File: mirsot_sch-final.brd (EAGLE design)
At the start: 79 x 79 mm, 42 parts, among them IC1 7805T, IC2 MEGA16-P, M1 WIRELESS-NRF24L01

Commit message: finalized pcb
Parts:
- removed CN2: (no value), adafruit:JST-PH-2-THM
- added J1: XT60-M, XT60-M:AMASS_XT60-M
- moved C8 19.3 mm to (66.1, 69.6), turned to 0 degrees
- moved C1 17.1 mm to (22.8, 23.5), turned to 0 degrees
- moved IC1 11.7 mm to (18.6, 9.52), turned to 180 degrees
- moved M1 9.76 mm to (70.0, 60.4), turned to 0 degrees
- moved C5 9.66 mm to (13.0, 19.8), turned to 180 degrees
- moved C4 2.55 mm to (10.0, 7.73)
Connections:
- net GND: now also J1.N; no longer CN2.2
- net VCC: now also J1.P; no longer CN2.1
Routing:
- net +5V_SUPPLY: track 80.8 -> 54.4 mm
- net VCC: track 85.7 -> 111.1 mm
- net GND: track 0.00 -> 11.5 mm
- net CE: track 40.5 -> 48.2 mm
- net SCK: track 35.1 -> 41.7 mm
- net IRQ: track 55.3 -> 51.8 mm
- net MISO: track 38.8 -> 41.2 mm
- net +3V3: track 118.9 -> 117.1 mm
- net CSN: track 56.8 -> 58.5 mm
- net BIN1: track 27.0 -> 28.5 mm
- net RX: track 90.5 -> 92.0 mm
- net MOSI: track 48.5 -> 47.6 mm
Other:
- outline, holes or cut-outs redrawn

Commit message: changed battery connecter orientation
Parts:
- removed J1: XT60-M, XT60-M:AMASS_XT60-M
- added U$1: T_PLUG_CONNECTOR_H, con-T-plug:T_PLUG_CONNECTOR_H
- IC1: value 7805T -> 7805DT; device linear:TO220H -> linear:TO252
- moved IC1 13.2 mm to (10.5, 19.9), turned to 90 degrees
- moved C8 12.5 mm to (53.9, 66.7), turned to 270 degrees
- moved C4 11.3 mm to (18.5, 15.3), turned to 90 degrees
- moved C5 5.74 mm to (18.5, 21.5), turned to 270 degrees
- moved C1 4.32 mm to (22.0, 19.2), turned to 90 degrees
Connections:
- net +5V_SUPPLY: now also IC1.2; no longer IC1.3
- net GND: now also IC1.3, U$1.P$1; no longer IC1.2, J1.N
- net VCC: now also U$1.P$2; no longer J1.P
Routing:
- net +5V: track 32.9 -> 68.6 mm, vias 6 -> 8
- net VCC: track 111.1 -> 80.6 mm, vias 0 -> 1
- net +5V_SUPPLY: track 54.4 -> 65.1 mm
- net GND: track 11.5 -> 18.1 mm, vias 0 -> 1
- net +3V3: track 117.1 -> 111.3 mm
- net AIN2: track 57.2 -> 61.3 mm
- net LED_1: track 21.8 -> 20.9 mm
- net CE: track 48.2 -> 47.4 mm
- net SCK: track 41.7 -> 41.1 mm
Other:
- outline, holes or cut-outs redrawn

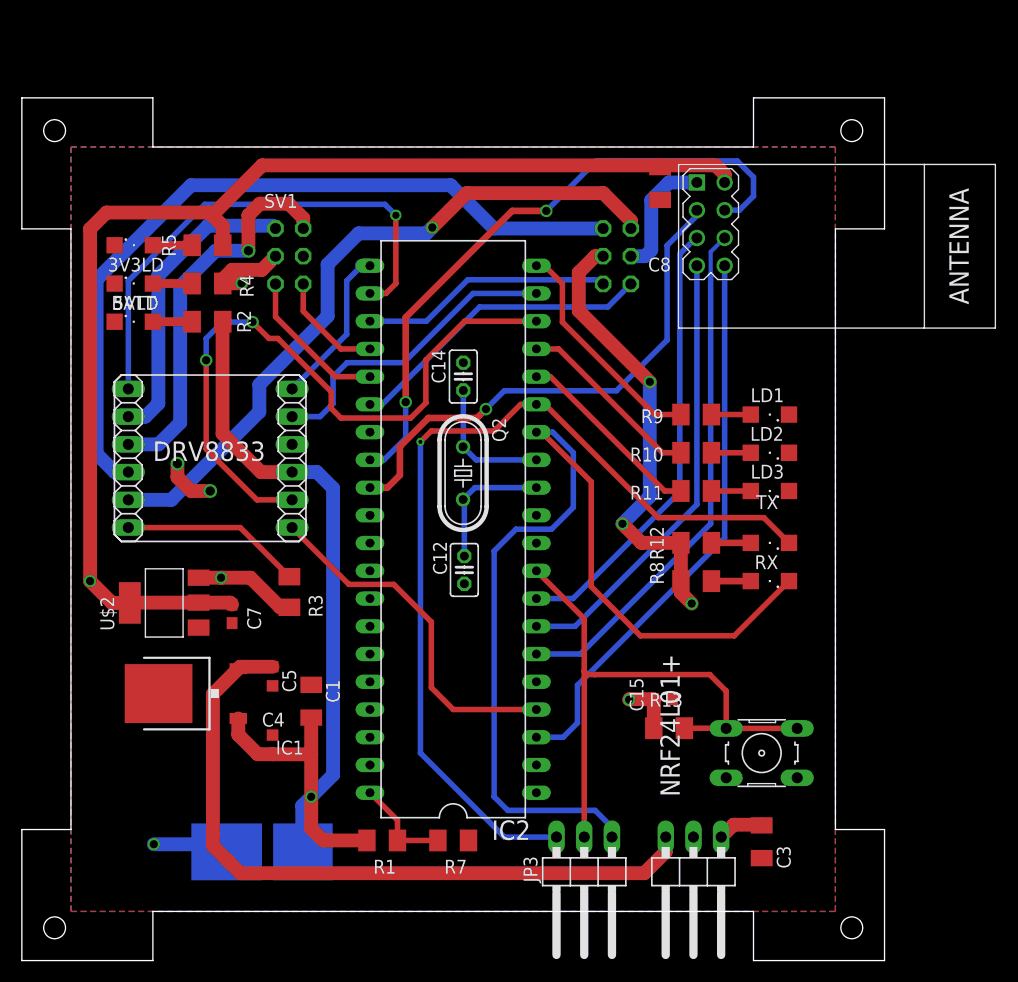
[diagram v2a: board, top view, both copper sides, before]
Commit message: changed mcu to esp32
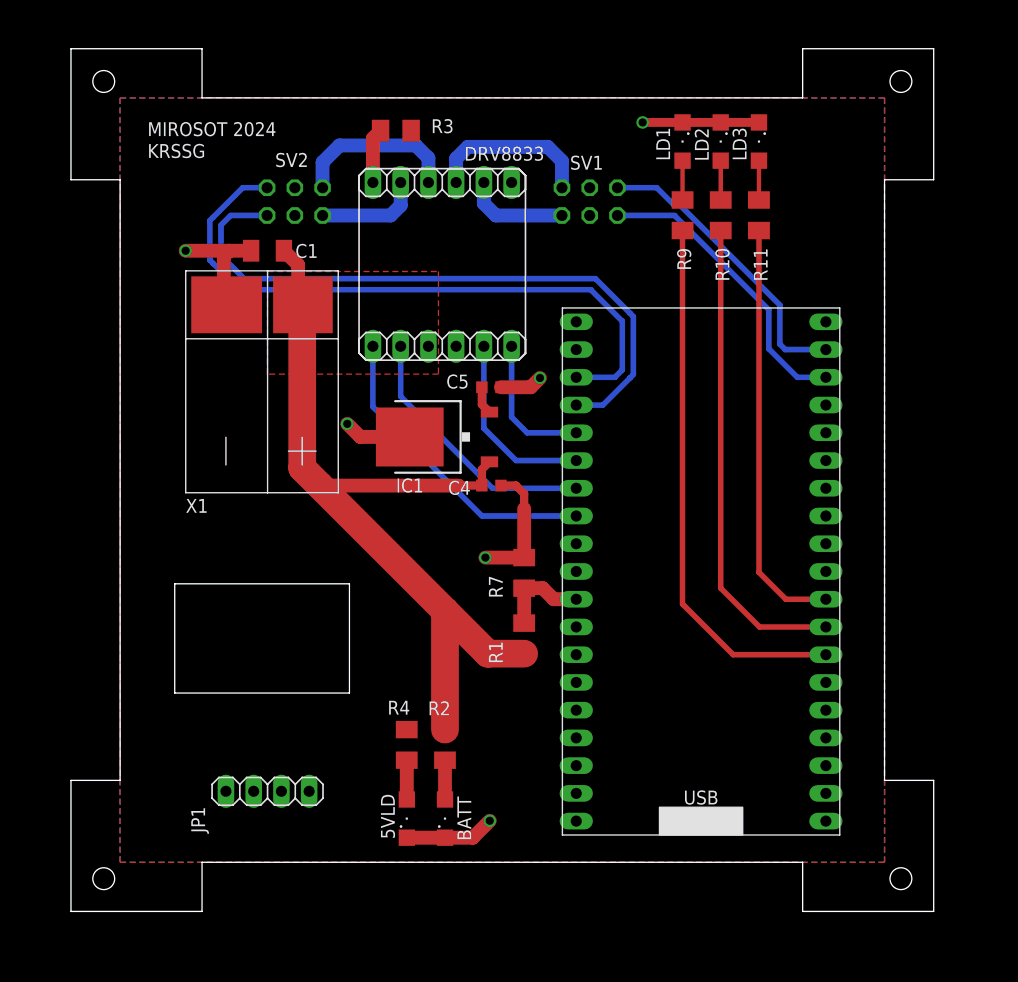
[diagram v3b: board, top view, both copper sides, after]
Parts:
- removed 3V3LD: RED, led:SML1206
- removed C12, C14: 22pF, rcl:C025-025X050
- removed C15: 100n, rcl:C0603K
- removed C3: 100n, rcl:C1206K
- removed C7: 100n, rcl:C0603
- removed C8: 10u, rcl:C1206K
- removed IC2: MEGA16-P, atmel:DIL40
- removed JP2, JP3: (no value), pinhead:1X03/90
- removed M1: WIRELESS-NRF24L01, diy-modules:WIRELESS-NRF24L01
- removed Q2: (no value), crystal:HC49/S
- removed R12, R5, R8: 330, rcl:M1206
- removed R13: 43k, rcl:M1206
- removed RX: BLUE, led:SML1206
- removed S2: (no value), switch-omron:B3F-10XX
- removed TX: YELLOW, led:SML1206
- added JP1: (no value), pinhead:1X04
- U$2: value LM1117-3.3 -> ESP32; device LM1117-3.3:SOT-223 -> ESP32:ESP32
- moved 5VLD 55.0 mm to (30.8, 8.50), turned to 90 degrees
- moved BATT 53.7 mm to (34.2, 8.50), turned to 90 degrees
- moved R4 46.0 mm to (30.8, 15.2), turned to 90 degrees
- moved R2 44.4 mm to (34.2, 15.2), turned to 90 degrees
- moved R3 43.4 mm to (29.8, 71.5), turned to 180 degrees
- moved U$2 42.2 mm to (45.0, 7.00), turned to 0 degrees
- moved C1 41.4 mm to (18.0, 60.5), turned to 180 degrees
- moved JP4 38.3 mm to (34.0, 66.8), turned to 180 degrees
- moved U$1 36.0 mm to (18.0, 48.5), flipped to the top, turned to 90 degrees
- moved C5 33.2 mm to (38.5, 48.0), turned to 0 degrees
- moved IC1 32.9 mm to (33.5, 43.5)
- moved LD3 32.0 mm to (63.0, 70.5), turned to 270 degrees
- moved C4 31.1 mm to (38.5, 39.0), turned to 0 degrees
- moved SV2 29.9 mm to (20.5, 65.0), turned to 0 degrees
- moved LD2 28.9 mm to (59.5, 70.5), turned to 270 degrees
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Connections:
- net AOUT+ renamed AOUT_P
- net AOUT- renamed AOUT_N
- net BOUT+ renamed BOUT_P
- net BOUT- renamed BOUT_N
- removed net +3V3: C7.1, C8.1, M1.2, R5.2, U$2.2, U$2.4
- removed net +5V_PROG: C3.1, JP2.1
- removed net +5V_SUPPLY: C5.1, IC1.2, JP2.3
- removed net CE: IC2.29, M1.3
- removed net CSN: IC2.28, M1.4
- removed net ENB: IC2.22, JP4.1
- removed net ENCD_MA_1: IC2.25, SV1.6
- removed net ENCD_MA_2: IC2.24, SV1.5
- removed net ENCD_MB_1: IC2.23, SV2.6
- removed net ENCD_MB_2: IC2.26, SV2.5
- removed net IRQ: IC2.3, M1.8
- removed net MISO: IC2.7, M1.7
- removed net MOSI: IC2.6, M1.6
- removed net N$10: R8.1, RX.A
- removed net N$11: R12.1, TX.A
- removed net N$12: C12.1, IC2.12, Q2.2
- removed net N$13: C14.1, IC2.13, Q2.1
- removed net N$6: 3V3LD.A, R5.1
- removed net RESET: IC2.9, JP3.2, R13.1, S2.3, S2.4
- removed net RX: IC2.14, JP3.1, RX.C
- removed net SCK: IC2.8, M1.5
- removed net TX: IC2.15, JP3.3, TX.C
- new net ENCD_MA_N: SV1.5, U$2.GPIO23
- new net ENCD_MA_P: SV1.6, U$2.GPIO22
- new net ENCD_MB_N: SV2.5, U$2.GPIO39
- new net ENCD_MB_P: SV2.6, U$2.GPIO36
- net +5V: now also C5.1, IC1.2, U$2.5V; no longer C15.1, IC2.10, IC2.30, IC2.32, JP2.2, R12.2, R13.2, R8.2, U$2.3
- net AIN1: now also U$2.GPIO33; no longer IC2.4
- net AIN2: now also U$2.GPIO32; no longer IC2.18
- net BIN1: now also U$2.GPIO35; no longer IC2.19
- net BIN2: now also U$2.GPIO34; no longer IC2.21
- net GND: now also U$2.GND1, U$2.GND2, U$2.GND3; no longer 3V3LD.C, C12.2, C14.2, C15.2, C3.2, C7.2, C8.2, IC2.11, IC2.31, M1.1, S2.1, S2.2, U$2.1
- net LED_1: now also U$2.GPIO4; no longer IC2.20
- net LED_2: now also U$2.GPIO16; no longer IC2.17
- net LED_3: now also U$2.GPIO17; no longer IC2.16
- net VCC_REF: now also U$2.GPIO27; no longer IC2.40
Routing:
- net +3V3: track 111.3 -> 0.00 mm, vias 1 -> 0
- net RX: track 92.0 -> 0.00 mm
- net TX: track 84.6 -> 0.00 mm, vias 1 -> 0
- net +5V: track 68.6 -> 2.56 mm, vias 8 -> 0
- net +5V_SUPPLY: track 65.1 -> 0.00 mm
- net ENCD_MB_N: track 0.00 -> 59.1 mm
- net ENCD_MB_P: track 0.00 -> 59.1 mm
- net CSN: track 58.5 -> 0.00 mm, vias 2 -> 0
- net BOUT_P: track 71.1 -> 15.4 mm
- net BOUT_N: track 63.7 -> 9.63 mm, vias 1 -> 0
- net RESET: track 53.7 -> 0.00 mm
- net IRQ: track 51.8 -> 0.00 mm
- net MOSI: track 47.6 -> 0.00 mm
- net CE: track 47.4 -> 0.00 mm, vias 1 -> 0
- net ENB: track 46.7 -> 0.00 mm, vias 1 -> 0
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- added copper zone on layer 1, net +5V
- added copper zone on layer 16, net GND
- added copper zone on layer 1, net VCC
- removed copper zone on layer 16, net +5V
- removed copper zone on layer 1, net GND
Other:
- outline, holes or cut-outs redrawn
- board text added: "KRSSG"
- board text added: "MIROSOT 2024"
- board text added: "X1"
- board text removed: "NRF24L01+"

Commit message: added level shifter, changed hole size, added switch
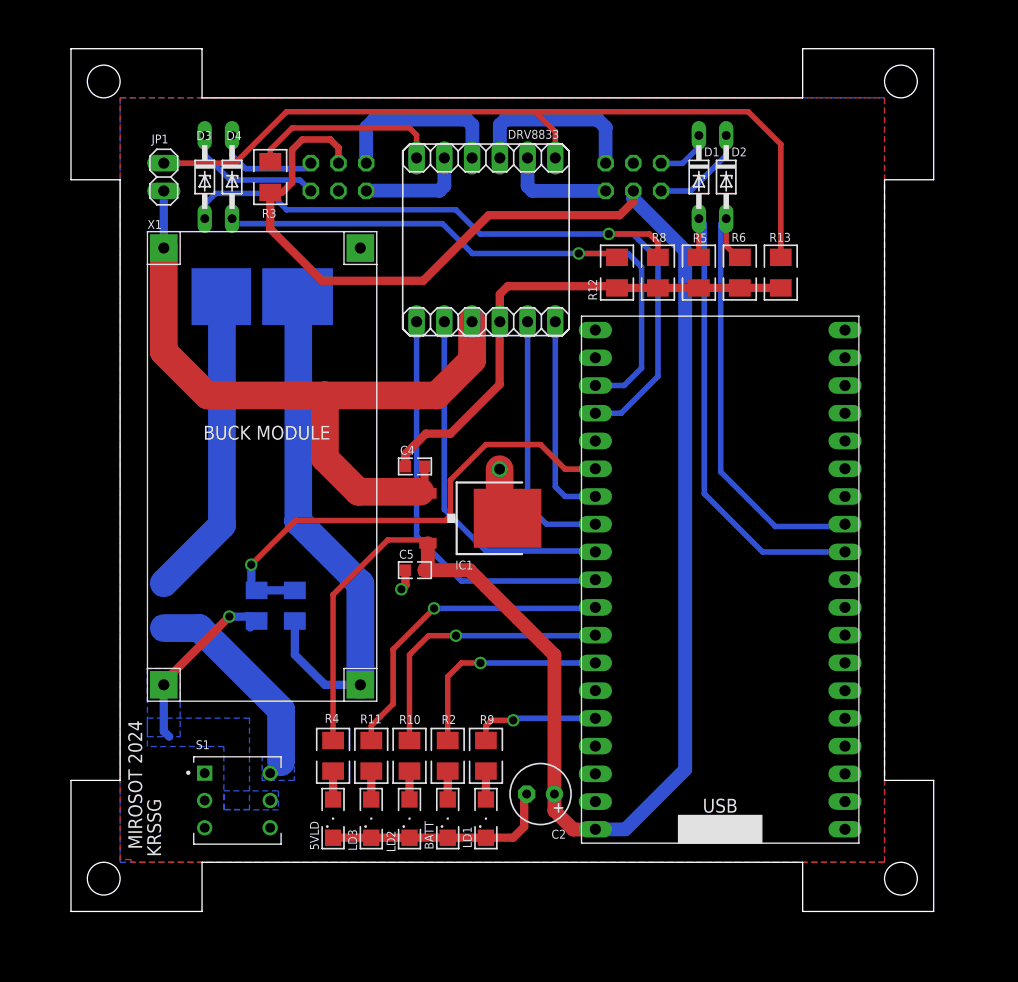
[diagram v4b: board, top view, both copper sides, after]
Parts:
- removed C1: 10u, rcl:C1206K
- added C2: (no value), rcl:E2,5-6
- added D1, D2, D3, D4: (no value), diode:DO34Z7
- added D5: M7, M7:DIOM505270X240
- added R12, R13, R5, R6, R8: 10K, rcl:M1206
- added S1: TL2285EE, TL2285EE:SW_TL2285EE
- added U$3: BUCK_CONVERTER, BUCK_CONVERTER:BUCK_CONVERTER
- JP1: device pinhead:1X04 -> pinhead:1X02
- moved LD3 71.4 mm to (27.5, 8.50), turned to 90 degrees
- moved LD2 68.2 mm to (31.0, 8.50), turned to 90 degrees
- moved LD1 64.6 mm to (38.0, 8.50), turned to 90 degrees
- moved R11 60.9 mm to (27.5, 14.2), turned to 90 degrees
- moved R10 57.1 mm to (31.0, 14.2), turned to 90 degrees
- moved JP1 57.0 mm to (8.50, 67.2), turned to 270 degrees
- moved R9 52.7 mm to (38.0, 14.2), turned to 90 degrees
- moved R1 24.7 mm to (17.0, 28.0), flipped to the bottom
- moved R7 21.2 mm to (20.5, 28.0), flipped to the bottom, turned to 90 degrees
- moved C5 18.2 mm to (31.5, 31.2), turned to 180 degrees
- moved R3 12.3 mm to (18.2, 67.2), turned to 90 degrees
- moved IC1 8.44 mm to (37.5, 36.0), turned to 270 degrees
- moved C4 7.22 mm to (31.5, 40.8), turned to 180 degrees
- moved R4 6.82 mm to (24.0, 14.2)
- moved 5VLD 6.75 mm to (24.0, 8.50)
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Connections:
- new net BATT_LED: R2.2, U$2.GPIO12
- new net N$10: D4.C, SV2.6
- new net N$11: D5.A, U$1.P$2
- new net N$13: JP1.1, JP4.1, R13.2
- new net N$14: D5.C, S1.4
- new net N$15: R1.2, S1.5, U$3.IN+
- new net N$16: R7.1, U$1.P$1, U$3.IN-
- new net N$6: D1.C, SV1.5
- new net N$7: D2.C, SV1.6
- new net N$8: D3.C, SV2.5
- net +5V: now also C2.+
- net AIN1: now also U$2.GPIO26; no longer U$2.GPIO33
- net AIN2: now also U$2.GPIO25; no longer U$2.GPIO32
- net BIN1: now also U$2.GPIO33; no longer U$2.GPIO35
- net BIN2: now also U$2.GPIO32; no longer U$2.GPIO34
- net ENCD_MA_N: now also D1.A, R5.2, U$2.GPIO18; no longer SV1.5, U$2.GPIO23
- net ENCD_MA_P: now also D2.A, R6.1, U$2.GPIO19; no longer SV1.6, U$2.GPIO22
- net ENCD_MB_N: now also D3.A, R8.2; no longer SV2.5
- net ENCD_MB_P: now also D4.A, R12.1; no longer SV2.6
- net GND: now also C2.-, R12.2, R13.1, R5.1, R6.2, R8.1, U$3.OUT-; no longer C1.2, R7.1, U$1.P$1
- net LED_1: now also U$2.GPIO13; no longer U$2.GPIO4
- net LED_2: now also U$2.GPIO14; no longer U$2.GPIO16
- net LED_3: now also U$2.GPIO27; no longer U$2.GPIO17
- net VCC: now also JP1.2, U$3.OUT+; no longer C1.1, R1.2, R2.2, U$1.P$2
- net VCC_REF: now also U$2.GPIO35; no longer U$2.GPIO27
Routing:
- net +5V: track 2.56 -> 188.2 mm
- net N$13: track 0.00 -> 75.0 mm
- net N$16: track 0.00 -> 47.4 mm
- net LED_1: track 49.3 -> 11.7 mm, vias 0 -> 1
- net VCC_REF: track 8.39 -> 45.6 mm, vias 0 -> 1
- net N$11: track 0.00 -> 27.5 mm
- net GND: track 52.8 -> 77.9 mm, vias 6 -> 2
- net N$14: track 0.00 -> 20.1 mm
- net BATT_LED: track 0.00 -> 19.9 mm, vias 0 -> 1
- net LED_2: track 43.9 -> 25.6 mm, vias 0 -> 1
- net N$15: track 0.00 -> 17.6 mm, vias 0 -> 1
- net ENCD_MA_N: track 27.3 -> 44.0 mm
- net ENCD_MA_P: track 27.3 -> 41.1 mm
- net N$8: track 0.00 -> 12.8 mm
- net N$1: track 5.04 -> 17.7 mm
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- added copper zone on layer 1, net GND
- added copper zone on layer 16, net N$14
- added copper zone on layer 16, net N$15
- removed copper zone on layer 1, net +5V
- removed copper zone on layer 1, net VCC
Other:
- outline, holes or cut-outs redrawn
